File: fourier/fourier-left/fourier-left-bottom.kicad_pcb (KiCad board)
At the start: 2 copper layers, 136.6 x 92.2 mm, 9 parts

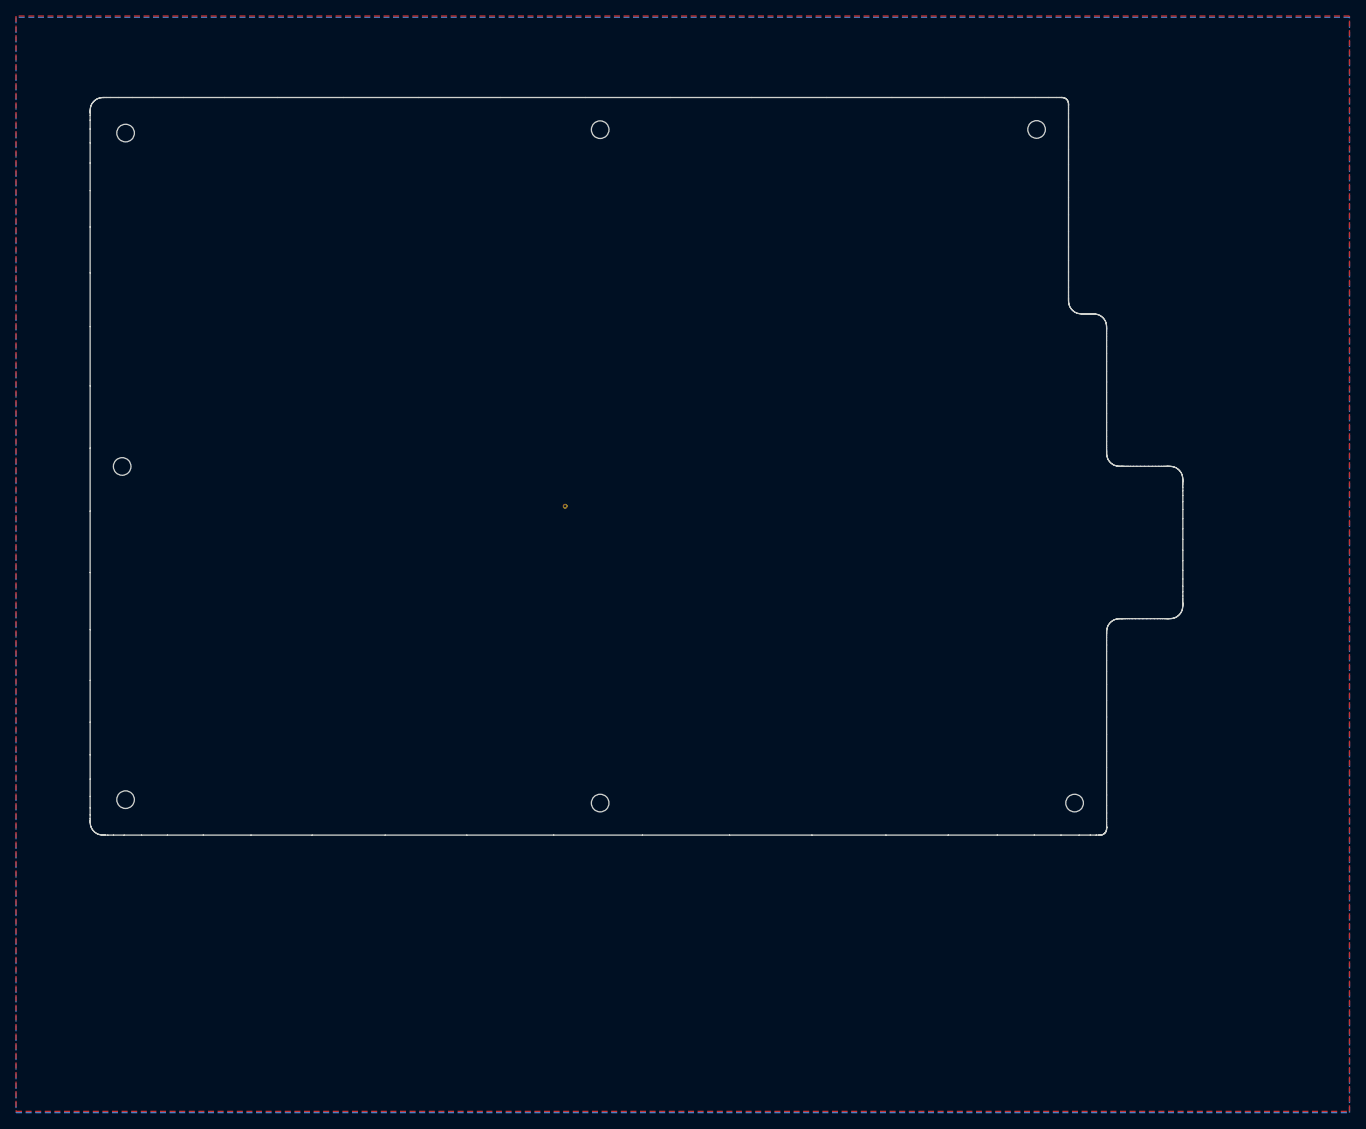
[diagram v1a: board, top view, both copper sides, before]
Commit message: Top height and center hole adjusment
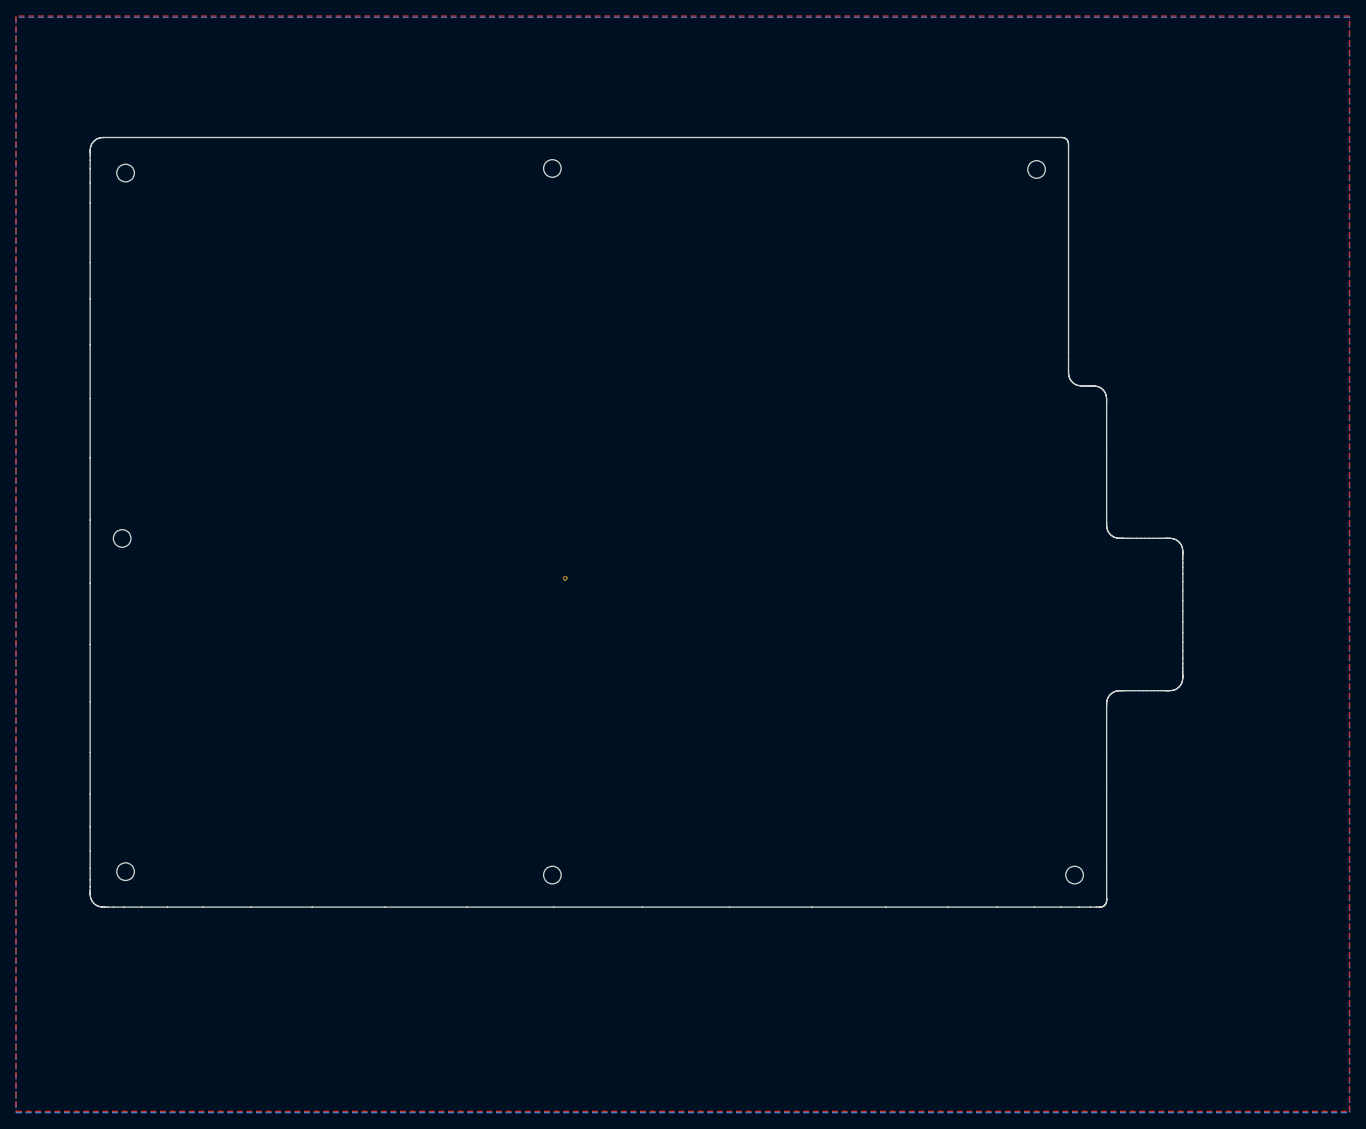
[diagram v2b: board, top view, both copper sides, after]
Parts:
- removed G***: LOGO, Keebio-Art:Keebio-TwoTone
- moved REF** 10.8 mm to (73.0, 112.3)
- moved REF** 9.00 mm to (19.2, 70.2)
- moved REF** 9.00 mm to (19.6, 111.9)
- moved REF** 9.00 mm to (138.3, 112.3)
- moved REF** 9.00 mm to (74.6, 75.2)
- moved REF** 7.70 mm to (73.0, 24.0)
- moved REF** 5.00 mm to (133.5, 24.1)
- moved REF** 5.00 mm to (19.6, 24.6)
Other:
- board size 136.6 x 92.2 mm -> 136.6 x 96.2 mm

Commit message: rotate left-top and update to KiCad 5.99
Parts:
- removed the REF** at (73.0, 24.0)
- removed the REF** at (73.0, 112.3)
- removed the REF** at (74.6, 75.2)
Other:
- net class Default removed
